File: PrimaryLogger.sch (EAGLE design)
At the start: 65 parts, among them J1 CONN_42.54_SCREW, J2 CONN_42.54_SCREW, J3 CONN_42.54_SCREW, J4 CONN_42.54_SCREW, J5 CONN_32.54_SCREW, Q1 DMG3404, Q2 DMG3404, U1 MIC2005, U2 MIC2091, U25 SN74AUP3G34DCU, U3 TPL5010DDC, U4 TXS0102DCU, U5 SN74LVC1G3157SC70, U6 TCS3400, U7 SHTC3DFN, U8 MCP23008QFN, U9 MCP7940SOIC

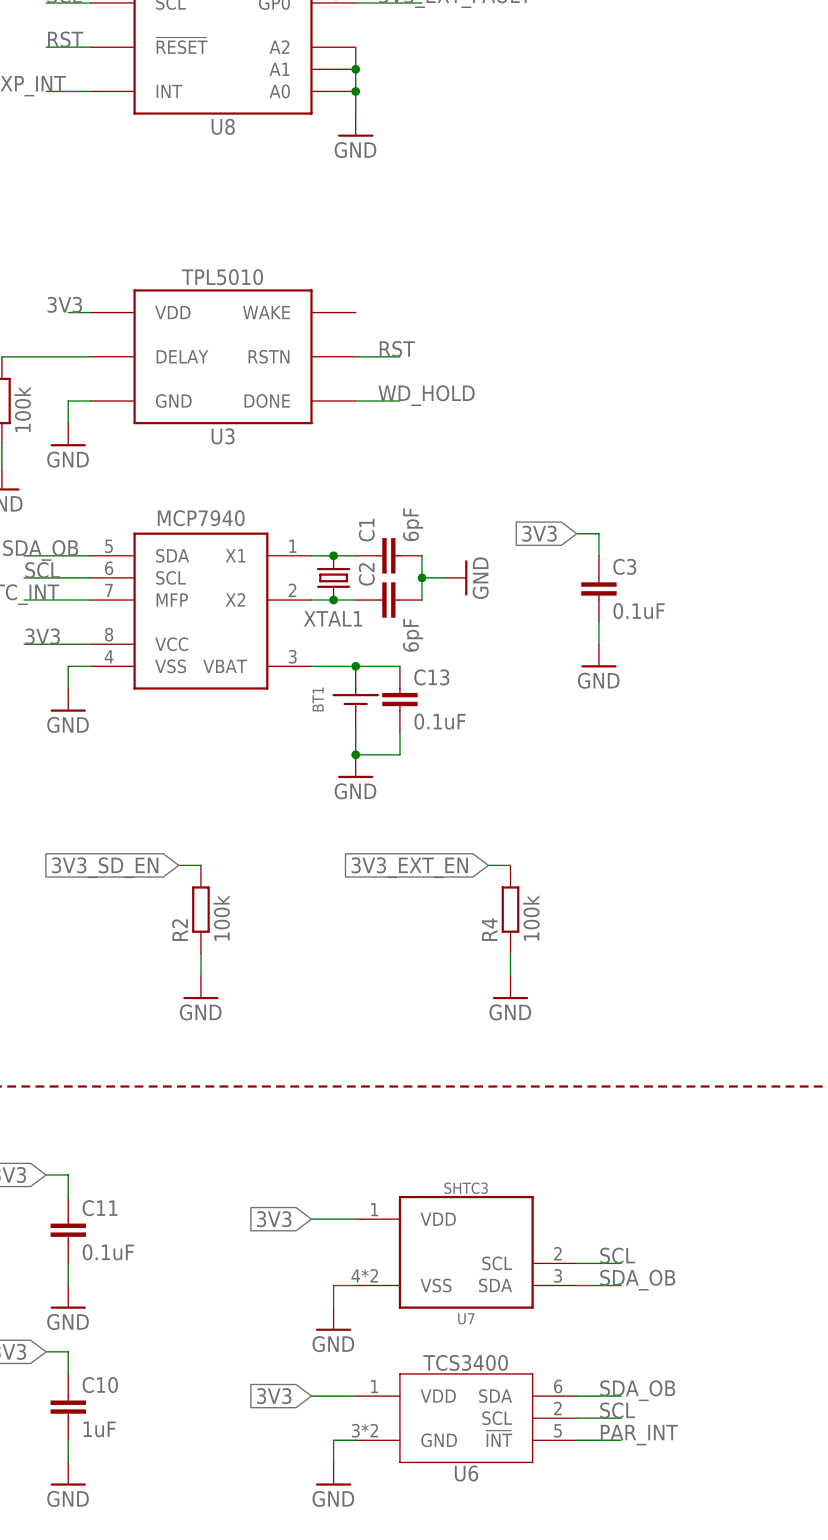
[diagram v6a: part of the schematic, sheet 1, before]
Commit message: Added I2C address info to schematic
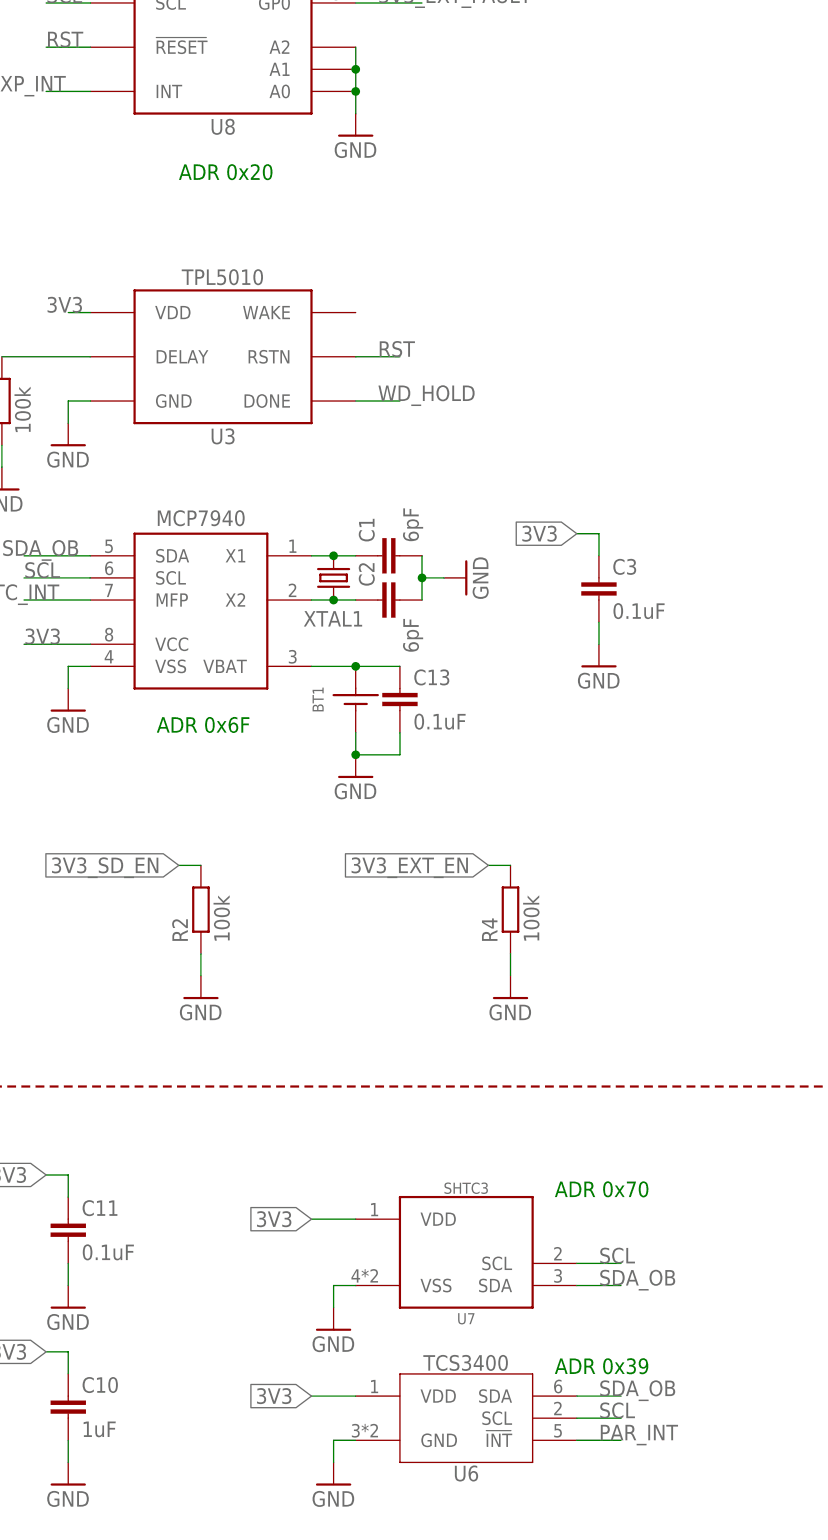
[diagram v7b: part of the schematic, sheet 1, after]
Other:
- note added: "ADR 0x20"
- note added: "ADR 0x39"
- note added: "ADR 0x6F"
- note added: "ADR 0x70"
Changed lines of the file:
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@@
 <setting verticaltext="up"/>
 </settings>
-<grid distance="0.1" unitdist="inch" unit="mm" style="lines" multiple="1" display="no" altdistance="0.01" altunitdist="inch" altunit="inch"/>
+<grid distance="0.1" unitdist="inch" unit="inch" style="lines" multiple="1" display="no" altdistance="0.01" altunitdist="inch" altunit="inch"/>
 <layers>
 <layer number="1" name="Top" color="4" fill="1" visible="no" active="no"/>
@@
 <text x="7.62" y="45.72" size="3.81" layer="91">Sensors</text>
 <text x="144.78" y="203.2" size="3.81" layer="91">Power</text>
+<text x="93.98" y="17.78" size="1.778" layer="91">ADR 0x39</text>
+<text x="93.98" y="38.1" size="1.778" layer="91">ADR 0x70</text>
+<text x="48.26" y="91.44" size="1.778" layer="91">ADR 0x6F</text>
+<text x="50.8" y="154.94" size="1.778" layer="91">ADR 0x20</text>
 </plain>
 <instances>

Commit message: Updated for v0.1, ready for fab
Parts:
- added C14: 0.1uF, bschulz_passives:C-EU0.1UFC0603
- added JP7: JUMPER-SMT_2_NC_PASTE_SILK, SparkFun-Jumpers:JUMPER-SMT_2_NC_PASTE_SILK
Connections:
- new net N$6: C14.1, JP7.1, U3.VDD
- new net WAKE: U3.WAKE, U8.GP5
- net 3V3: now also JP7.2; no longer U3.VDD
- net GND: now also C14.2
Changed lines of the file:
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@@
 <?xml version="1.0" encoding="utf-8"?>
 <!DOCTYPE eagle SYSTEM "eagle.dtd">
-<eagle version="9.5.2">
+<eagle version="9.4.2">
 <drawing>
 <settings>
@@
 <attribute name="REV" value="0.0"/>
 </part>
+<part name="C14" library="bschulz_passives" deviceset="C-EU" device="C0603" technology="0.1UF" value="0.1uF"/>
+<part name="JP7" library="SparkFun-Jumpers" library_urn="urn:adsk.eagle:library:528" deviceset="JUMPER-SMT_2_NC_PASTE" device="_SILK" package3d_urn="urn:adsk.eagle:package:39282/1"/>
+<part name="GND23" library="supply1" library_urn="urn:adsk.eagle:library:371" deviceset="GND" device=""/>
 </parts>
 <sheets>
@@
 <attribute name="REV" x="261.62" y="7.62" size="2.54" layer="94"/>
 </instance>
+<instance part="C14" gate="G$1" x="20.32" y="137.16" smashed="yes">
+<attribute name="NAME" x="21.844" y="137.541" size="1.778" layer="95"/>
+<attribute name="VALUE" x="21.844" y="132.461" size="1.778" layer="96"/>
+</instance>
+<instance part="JP7" gate="G$1" x="30.48" y="144.78" smashed="yes" rot="R90">
+<attribute name="NAME" x="27.94" y="142.24" size="1.778" layer="95" font="vector" rot="R90"/>
+<attribute name="VALUE" x="33.02" y="142.24" size="1.778" layer="96" font="vector" rot="R90" align="top-left"/>
+</instance>
+<instance part="GND23" gate="1" x="20.32" y="127" smashed="yes">
+<attribute name="VALUE" x="17.78" y="124.46" size="1.778" layer="96"/>
+</instance>
 </instances>
 <busses>
@@
 <label x="231.14" y="101.6" size="1.778" layer="95" xref="yes"/>
 </segment>
+<segment>
+<pinref part="C14" gate="G$1" pin="2"/>
+<wire x1="20.32" y1="132.08" x2="20.32" y2="129.54" width="0.1524" layer="91"/>
+<pinref part="GND23" gate="1" pin="GND"/>
+</segment>
 </net>
 <net name="SCL" class="0">
@@
 <wire x1="40.64" y1="101.6" x2="33.02" y2="101.6" width="0.1524" layer="91"/>
 <label x="33.02" y="101.6" size="1.778" layer="95"/>
-</segment>
-<segment>
-<pinref part="U3" gate="G$1" pin="VDD"/>
-<wire x1="40.64" y1="139.7" x2="38.1" y2="139.7" width="0.1524" layer="91"/>
-<label x="35.56" y="139.7" size="1.778" layer="95"/>
 </segment>
 <segment>
@@
 <label x="25.4" y="195.58" size="1.778" layer="95" rot="R180" xref="yes"/>
 </segment>
+<segment>
+<pinref part="JP7" gate="G$1" pin="2"/>
+<wire x1="30.48" y1="149.86" x2="30.48" y2="152.4" width="0.1524" layer="91"/>
+<wire x1="30.48" y1="152.4" x2="27.94" y2="152.4" width="0.1524" layer="91"/>
+<label x="27.94" y="152.4" size="1.778" layer="95" rot="R180" xref="yes"/>
+</segment>
 </net>
 <net name="RST" class="0">
@@
 </segment>
 </net>
+<net name="N$6" class="0">
+<segment>
+<pinref part="C14" gate="G$1" pin="1"/>
+<pinref part="JP7" gate="G$1" pin="1"/>
+<wire x1="20.32" y1="139.7" x2="30.48" y2="139.7" width="0.1524" layer="91"/>
+<pinref part="U3" gate="G$1" pin="VDD"/>
+<wire x1="30.48" y1="139.7" x2="40.64" y2="139.7" width="0.1524" layer="91"/>
+<junction x="30.48" y="139.7"/>
+</segment>
+</net>
+<net name="WAKE" class="0">
+<segment>
+<pinref part="U3" gate="G$1" pin="WAKE"/>
+<wire x1="71.12" y1="139.7" x2="76.2" y2="139.7" width="0.1524" layer="91"/>
+<label x="73.66" y="139.7" size="1.778" layer="95"/>
+</segment>
+<segment>
+<pinref part="U8" gate="G$1" pin="GP5"/>
+<wire x1="71.12" y1="187.96" x2="78.74" y2="187.96" width="0.1524" layer="91"/>
+<label x="73.66" y="187.96" size="1.778" layer="95"/>
+</segment>
+</net>
